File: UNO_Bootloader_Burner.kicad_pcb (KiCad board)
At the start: 2 copper layers, 57.9 x 53.3 mm, 12 parts, among them J1 Conn_01x06_Female, J2 Conn_01x06_Female, U1 ATmega328-AU-MCU_Microchip_AT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, Y1 Crystal_GND24

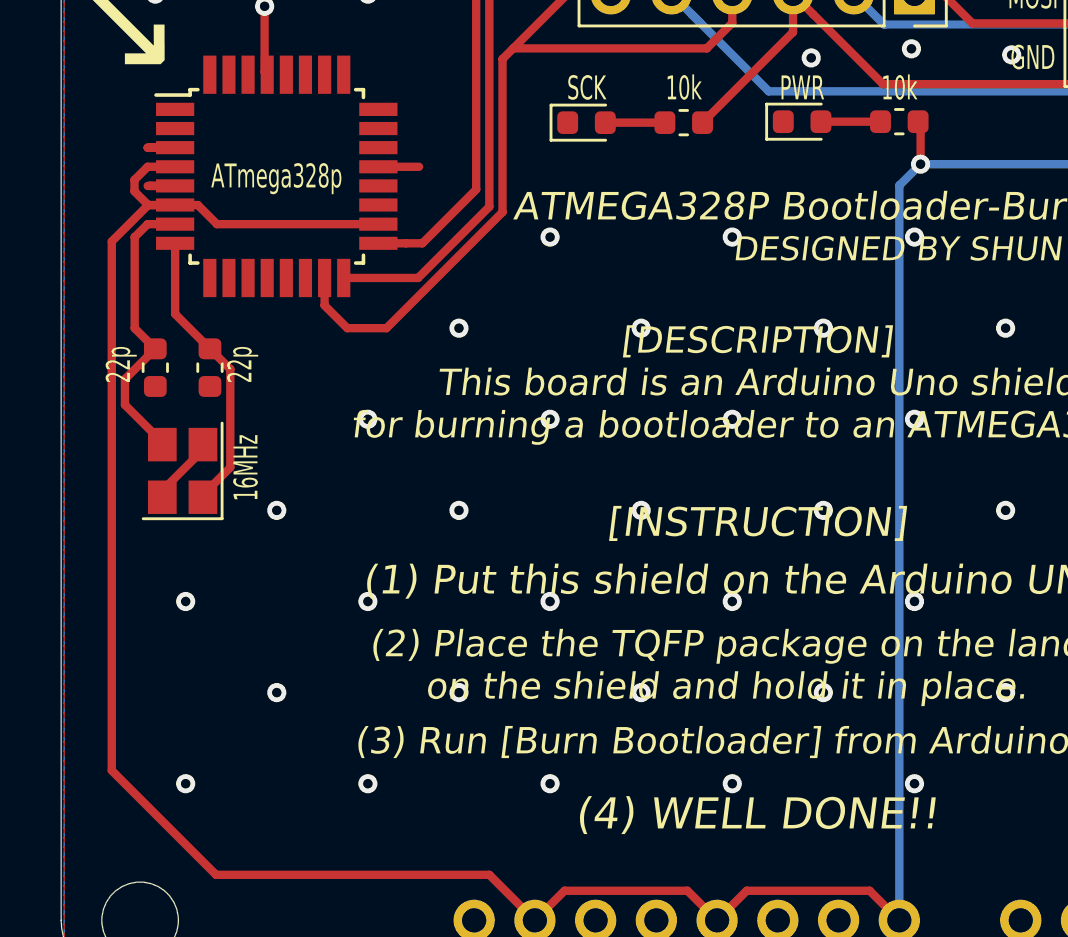
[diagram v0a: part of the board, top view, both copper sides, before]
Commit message: add QR CODE to the PCB file
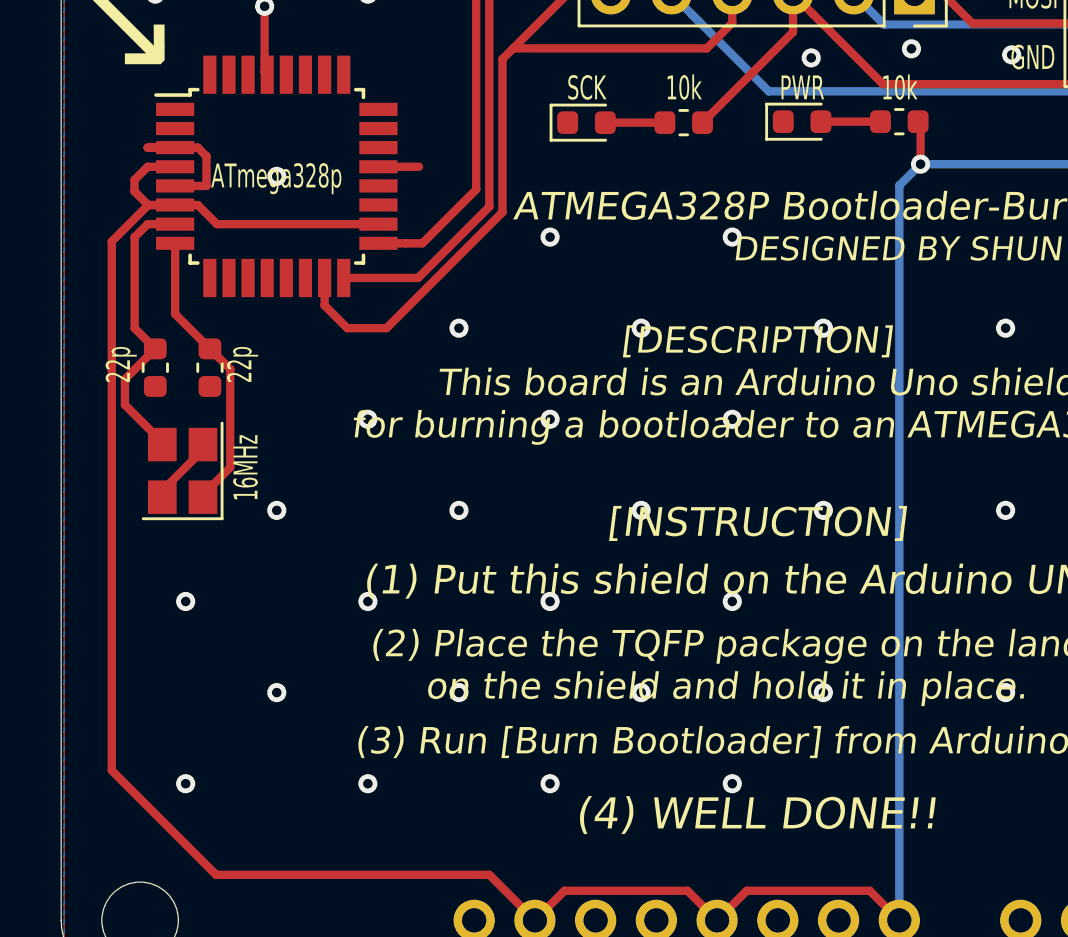
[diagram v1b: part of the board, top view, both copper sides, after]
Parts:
- added G***: LOGO, RobotClub_footprint:GitHub_QR_UNO_Bootloader_Burner, B.Cu at (156.0, 75.7)
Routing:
- net GND: track 9.16 -> 10.9 mm, vias 59 -> 56

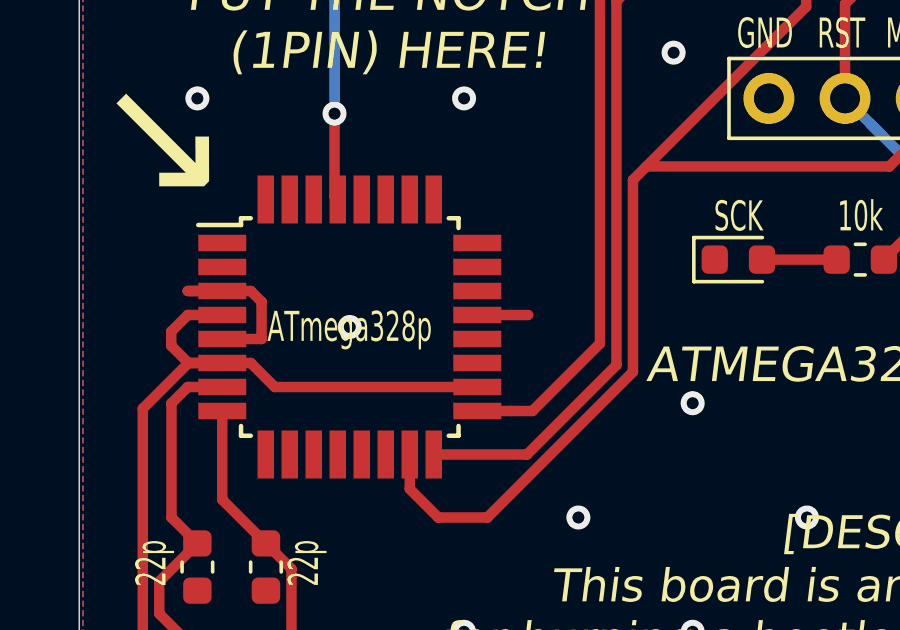
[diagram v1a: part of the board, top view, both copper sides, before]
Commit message: update library path
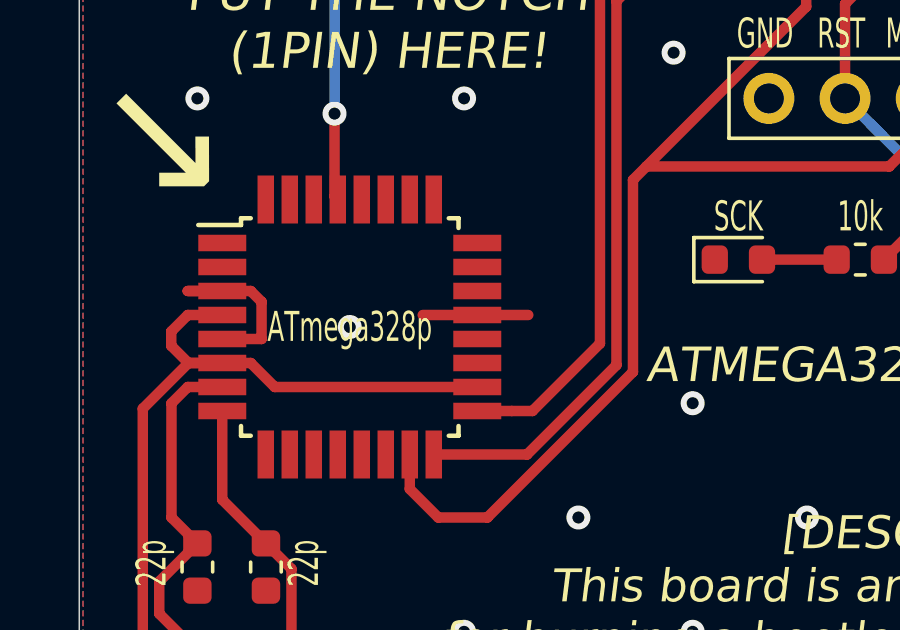
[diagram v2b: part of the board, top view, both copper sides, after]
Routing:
- net GND: track 10.9 -> 12.7 mm

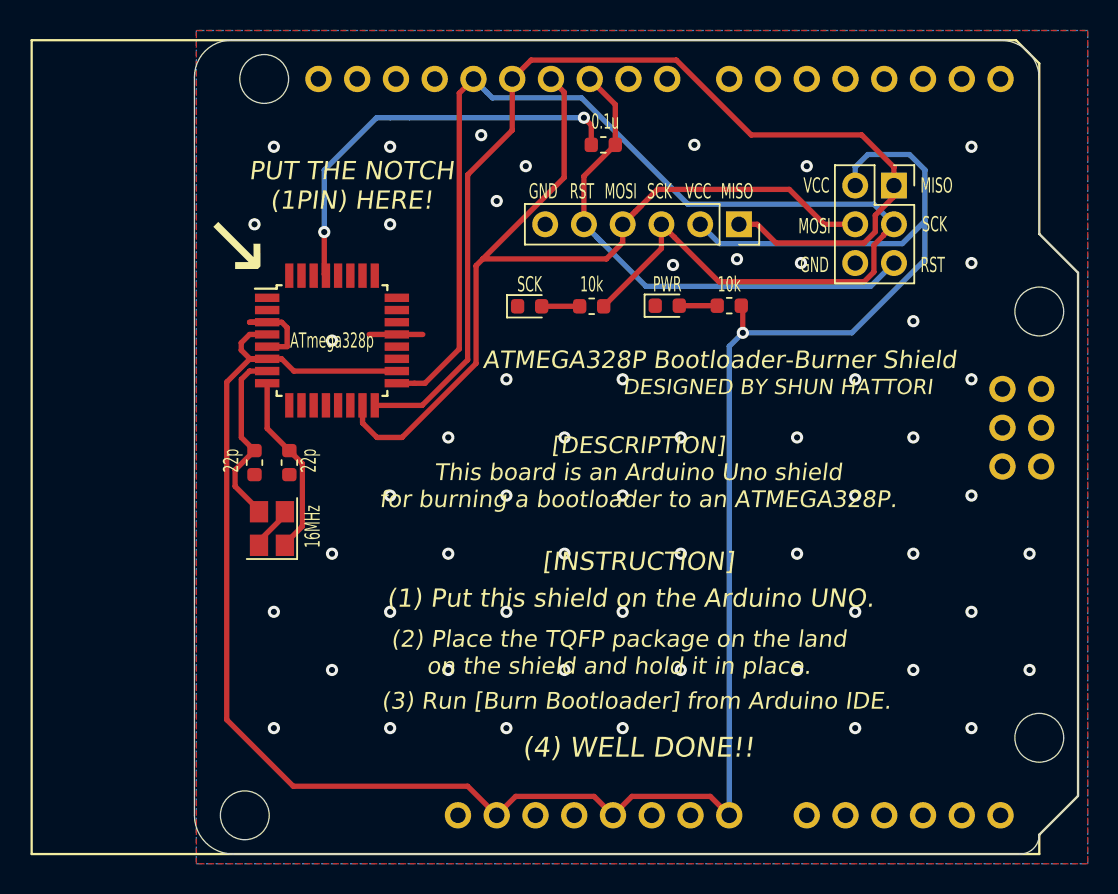
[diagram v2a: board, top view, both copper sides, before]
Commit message: change osc component, update osc pattern
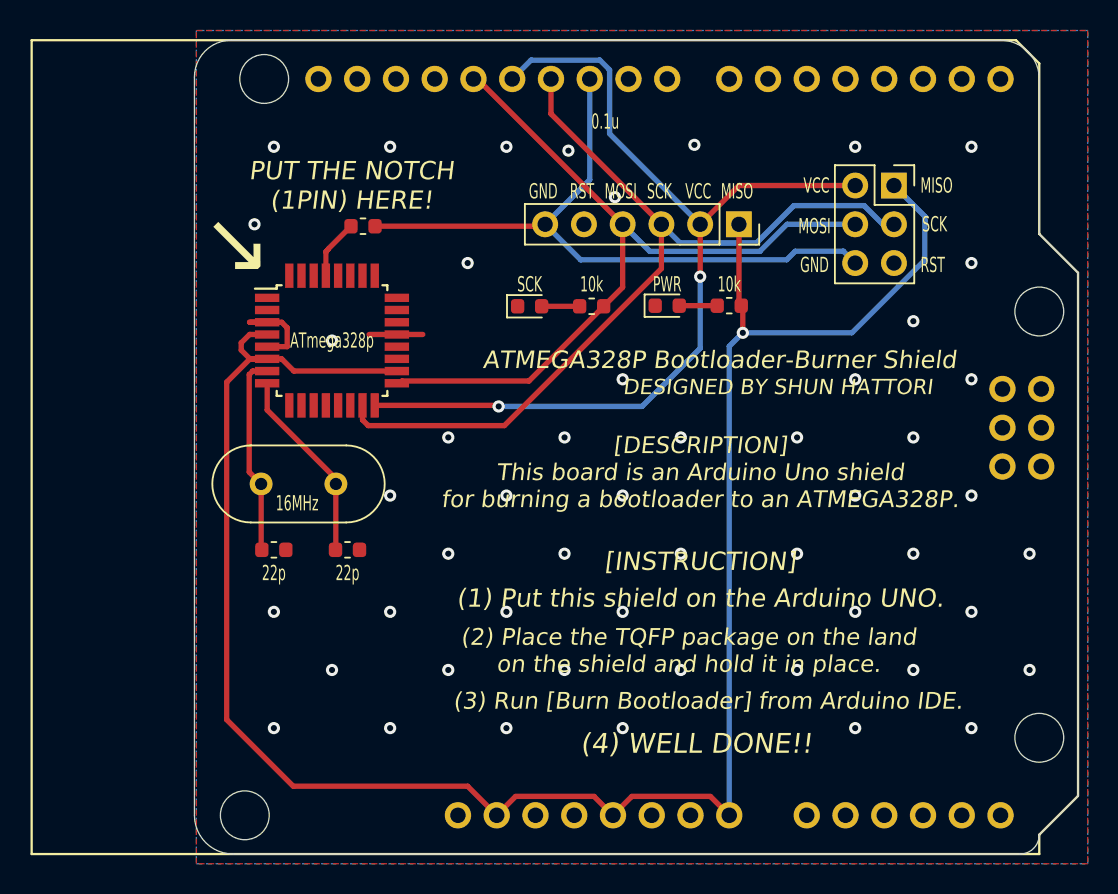
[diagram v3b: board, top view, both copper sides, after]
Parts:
- Y1: value Crystal_GND24 -> Crystal; footprint Crystal:Crystal_SMD_3225-4Pin_3.2x2.5mm -> Crystal:Crystal_HC18-U_Vertical
- moved C3 16.6 mm to (155.7, 63.6)
- moved C1 6.87 mm to (154.7, 84.8), turned to 0 degrees
- moved C2 5.85 mm to (149.9, 84.8), turned to 0 degrees
- moved Y1 5.11 mm to (153.9, 80.5), turned to 180 degrees
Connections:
- J1 pad 1: MISO_M -> VCC
- J1 pad 2: VCC -> MISO_M
- J1 pad 3: SCK_M -> MOSI_M
- J1 pad 4: MOSI_M -> SCK_M
- J1 pad 5: RESET_FROM_BURNER -> GND
- J1 pad 6: GND -> RESET_FROM_BURNER
- J2 pad 1: MISO_M -> VCC
- J2 pad 2: VCC -> MISO_M
- J2 pad 3: SCK_M -> MOSI_M
- J2 pad 4: MOSI_M -> SCK_M
- J2 pad 5: RESET_FROM_BURNER -> GND
- J2 pad 6: GND -> RESET_FROM_BURNER
- Y1 pad 2: GND -> Net-(C2-Pad1)
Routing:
- net SCK_M: track 81.0 -> 52.0 mm
- net RESET_S: track 27.4 -> 3.92 mm, vias 2 -> 0
- net VCC: track 152.2 -> 135.0 mm
- net RESET_FROM_BURNER: track 34.2 -> 43.8 mm
- net MISO_M: track 69.9 -> 62.0 mm, vias 0 -> 2
- net MOSI_M: track 62.1 -> 57.7 mm
- net GND: track 12.7 -> 9.83 mm, vias 56 -> 51
- net Net-(C2-Pad1): track 12.1 -> 13.1 mm
- net Net-(C1-Pad1): track 12.0 -> 12.8 mm
